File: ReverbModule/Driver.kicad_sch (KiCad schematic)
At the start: 5 parts, among them U1 NE5532

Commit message: In work
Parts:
- added C3, C4, C5, C6: 100nF, Capacitor_SMD:C_0805_2012Metric_Pad1.18x1.45mm_HandSolder, symbol Device:C
- added R3: 20K, symbol Device:R_US
- added RV1: R_Potentiometer_US, symbol Device:R_Potentiometer_US
- added U2: NE5532, symbol Amplifier_Operational:NE5532
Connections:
- net +15V: now also C3.1, C5.1, U2.8 (V+)
- net -15V: now also C4.2, C6.2, U2.4 (V-)
- net GND: now also C3.2, C4.1, C5.2, C6.1, RV1.3
- net at C2.2: now also R3.1, RV1.1
- new net Dry: R3.2
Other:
- title: (none) -> Reverb Driver
- moved on the sheet: C2, U1C

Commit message: In progress
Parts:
- added C7: 100nF, Capacitor_SMD:C_0805_2012Metric_Pad1.18x1.45mm_HandSolder, symbol Device:C
- added R4: 10k, Resistor_SMD:R_0805_2012Metric_Pad1.20x1.40mm_HandSolder, symbol Device:R_US
- added RV2: 20k, symbol Device:R_Potentiometer_Trim_US
- RV1: value R_Potentiometer_US -> 10k
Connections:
- net GND: now also R4.1, RV2.3
- net at U1.5 (+): now also R4.2, RV2.2
- net ToLimiter: now reaches RV1.2
- new net: C7.2, RV2.1
- new net FromLimiter: C7.1
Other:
- note added: "Drive Level"
- moved on the sheet: U1B

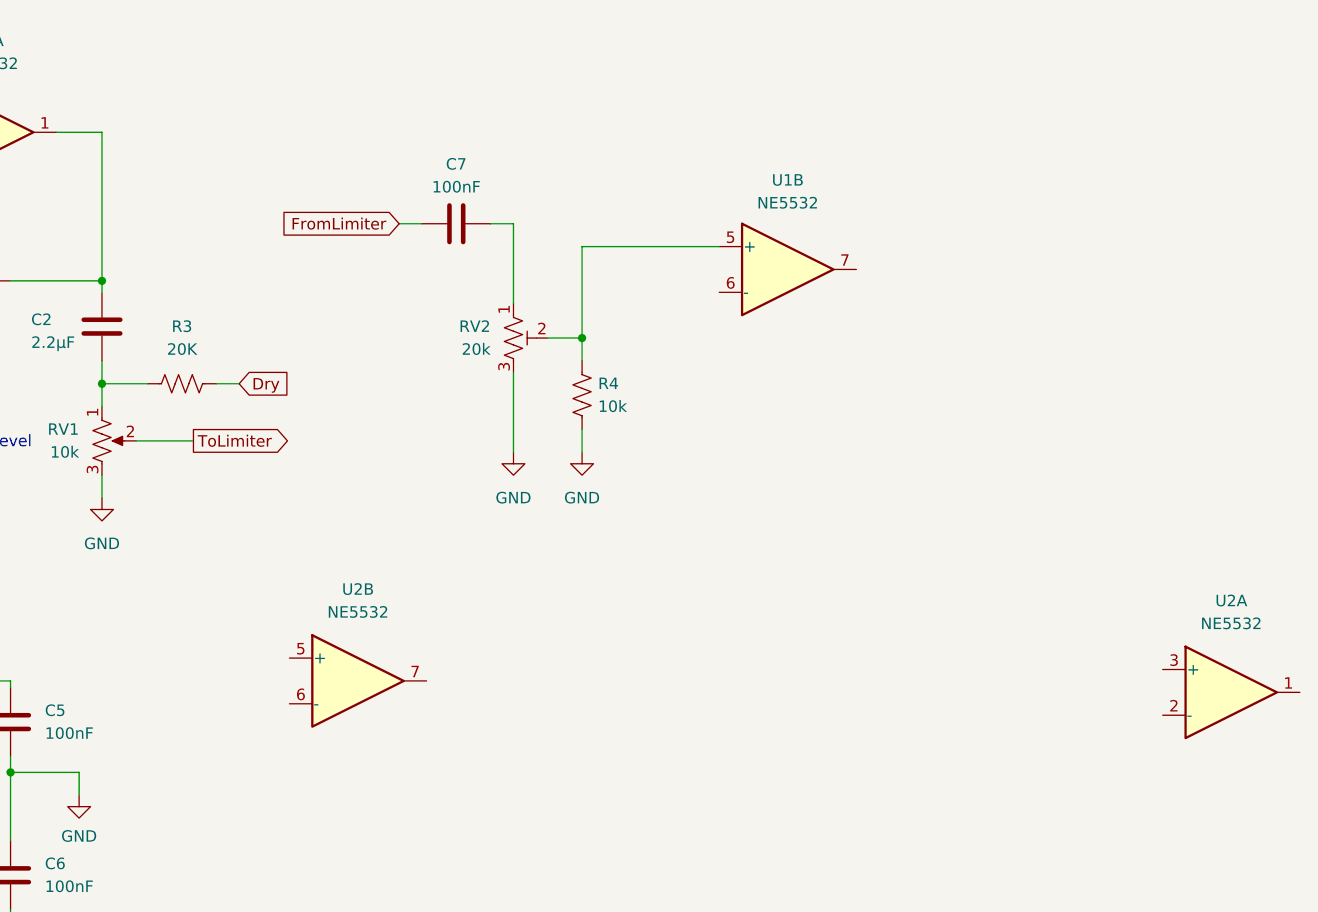
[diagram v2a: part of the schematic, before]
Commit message: added more parts
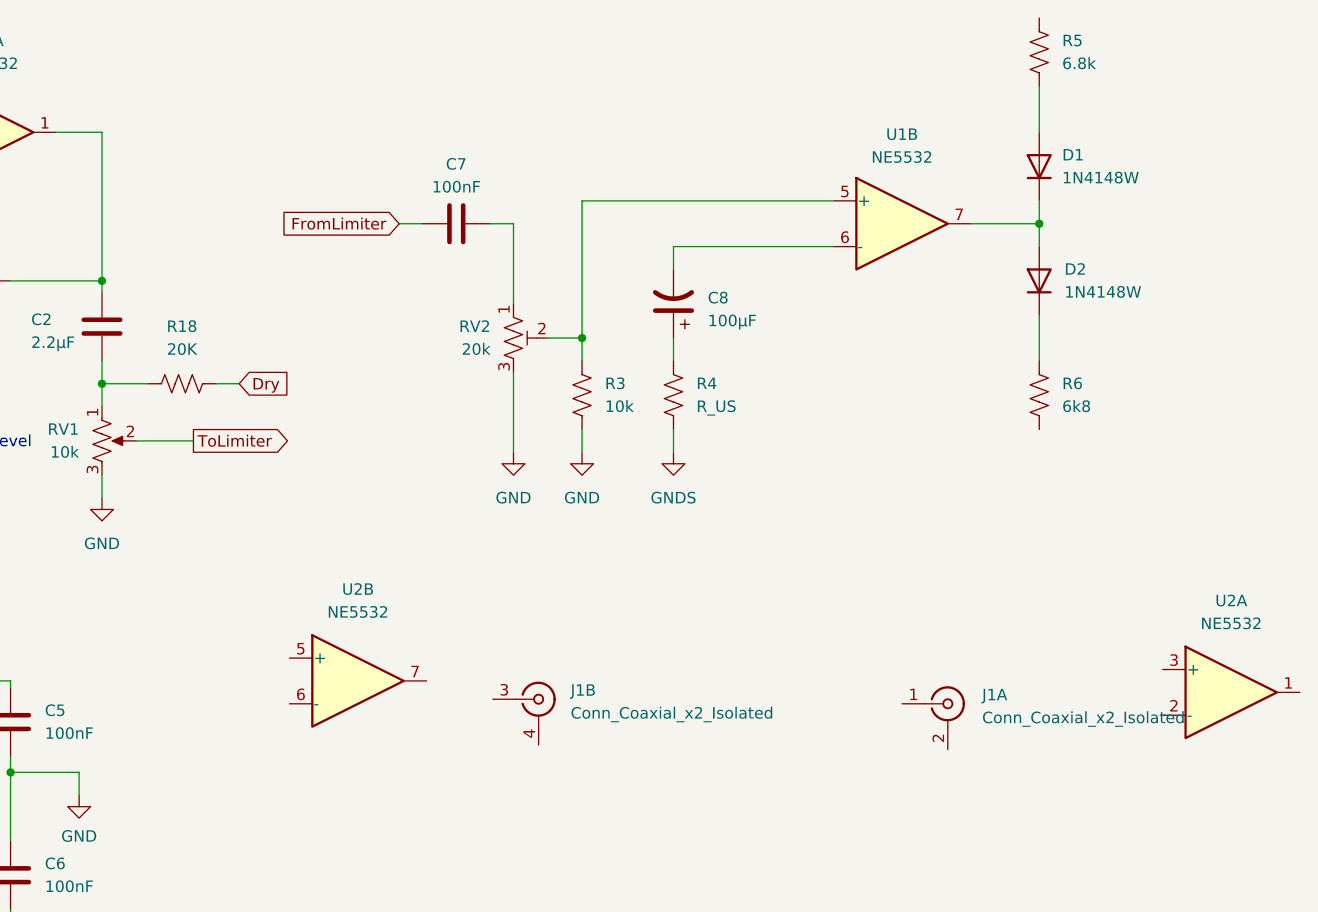
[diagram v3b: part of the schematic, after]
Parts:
- added C8: 100µF, symbol Device:C_Polarized_US
- added D1, D2: 1N4148W, Diode_SMD:D_SOD-123, symbol Diode:1N4148W
- added J1: Conn_Coaxial_x2_Isolated, symbol Connector:Conn_Coaxial_x2_Isolated
- added R4: R_US, symbol Device:R_US
- added R5: 6.8k, Resistor_SMD:R_0805_2012Metric_Pad1.20x1.40mm_HandSolder, symbol Device:R_US
- added R6: 6k8, Resistor_SMD:R_0805_2012Metric_Pad1.20x1.40mm_HandSolder, symbol Device:R_US
- renumbered R3 to R18, R4 to R3
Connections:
- net at U1.6 (-): now also C8.2
- net at U1.7: now also D1.1 (K), D2.2 (A)
- new net: C8.1, R4.1
- new net: D2.1 (K), R6.1
- new net: D1.2 (A), R5.2
- new net GNDS: R4.2
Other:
- moved on the sheet: U1B

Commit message: In worl
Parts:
- removed C1: 2.2µF, Capacitor_SMD:C_1206_3216Metric_Pad1.33x1.80mm_HandSolder, symbol Device:C
- removed unit 2 of J1
- removed unit 2 of U2
- removed unit 1 of U2
- added C1, C10, C9: 10µF, Capacitor_SMD:CP_Elec_5x5.3, symbol Device:C_Polarized_US
- added Q1: BD139, Package_TO_SOT_THT:TO-126-3_Vertical, symbol Transistor_BJT:BD139
- added Q2: BD140, Package_TO_SOT_THT:TO-126-3_Vertical, symbol Transistor_BJT:BD140
- added R7, R8: 10, Resistor_SMD:R_1206_3216Metric_Pad1.30x1.75mm_HandSolder, symbol Device:R_US
- added R9: R_US, symbol Device:R_US
- J1: value Conn_Coaxial_x2_Isolated -> Tank
- R4: value R_US -> 33
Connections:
- net +15V: now also R5.1, Q1.2 (C)
- net -15V: now also R6.2, Q2.1 (E)
- net at C8.2, U1.6 (-): now also R9.2
- net at D1.1 (K), D2.2 (A), U1.7: now also J1.1 (In1), C10.1, C9.2, R7.2, R8.1, R9.1
- net at C8.1, R4.1: now also J1.2 (Ext1)
- net at D2.1 (K), R6.1: now also C10.2, Q2.3 (B)
- net at R1.1: now also C1.2
- net at D1.2 (A), R5.2: now also C9.1, Q1.3 (B)
- new net: Q1.1 (E), R7.1
- new net: Q2.2 (C), R8.2
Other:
- note added: "Tank Input must be floating"
- note added: "pre-order part"
- moved on the sheet: J1A

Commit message: More Schematic Capture
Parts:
- removed C5, C6: 100nF, Capacitor_SMD:C_0805_2012Metric_Pad1.18x1.45mm_HandSolder, symbol Device:C
- removed U2: NE5532, symbol Amplifier_Operational:NE5532
- added C11, C12: 10µF, Capacitor_SMD:CP_Elec_5x5.3, symbol Device:C_Polarized_US
- added J2: Screw_Terminal_01x02, symbol Connector:Screw_Terminal_01x02
- R4: footprint (none) -> Resistor_SMD:R_2512_6332Metric_Pad1.40x3.35mm_HandSolder; LCSC (none) -> C53728; MPN (none) -> 25121WF330JT4E
- R9: value R_US -> 150; footprint (none) -> Resistor_SMD:R_2512_6332Metric_Pad1.40x3.35mm_HandSolder; LCSC (none) -> C25471; MPN (none) -> 25121WJ0151T4E
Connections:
- net +15V: now also C11.1
- net -15V: now also C12.2
- net GND: no longer C3.2, C4.1
- net GNDS: now also C3.2, C4.1, C11.2, C12.1
- net at C1.1: now also J2.2 (Pin_2)
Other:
- moved on the sheet: R9

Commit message: Schematic Capture
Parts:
- J2: footprint (none) -> TerminalBlock_Phoenix:TerminalBlock_Phoenix_MKDS-3-2-5.08_1x02_P5.08mm_Horizontal
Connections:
- net ToLimiter is gone; now on an unnamed net: RV1.2
- net GND: now also J2.1 (Pin_1)
- net FromLimiter: no longer names the net of C7.1
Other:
- moved on the sheet: U1C
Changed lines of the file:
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@@
 	)
 	(junction
-		(at 38.1 119.38)
+		(at 38.1 139.7)
 		(diameter 0)
 		(color 0 0 0 0)
@@
 	)
 	(junction
-		(at 200.66 63.5)
+		(at 38.1 116.84)
 		(diameter 0)
 		(color 0 0 0 0)
 	)
 	(junction
-		(at 203.2 88.9)
+		(at 200.66 63.5)
 		(diameter 0)
 		(color 0 0 0 0)
 	)
 	(junction
-		(at 38.1 142.24)
+		(at 203.2 88.9)
 		(diameter 0)
 		(color 0 0 0 0)
 	)
 	(junction
-		(at 38.1 116.84)
+		(at 38.1 142.24)
 		(diameter 0)
 		(color 0 0 0 0)
@@
 	)
 	(junction
-		(at 38.1 139.7)
-		(diameter 0)
-		(color 0 0 0 0)
-	)
-	(junction
 		(at 60.96 127)
 		(diameter 0)
@@
 	(wire
 		(pts
+			(xy 33.02 72.39) (xy 33.02 76.2)
+		)
+		(stroke
+			(width 0)
+			(type default)
+		)
+	)
+	(wire
+		(pts
+			(xy 114.3 63.5) (xy 114.3 87.63)
+		)
+		(stroke
+			(width 0)
+			(type default)
+		)
+	)
+	(wire
+		(pts
 			(xy 81.28 69.85) (xy 81.28 53.34)
 		)
@@
 	(wire
 		(pts
-			(xy 85.09 87.63) (xy 91.44 87.63)
+			(xy 85.09 87.63) (xy 114.3 87.63)
 		)
 		(stroke
@@
 	(wire
 		(pts
-			(xy 38.1 116.84) (xy 38.1 119.38)
+			(xy 53.34 50.8) (xy 53.34 53.34)
 		)
 		(stroke
@@
 	(wire
 		(pts
-			(xy 53.34 50.8) (xy 53.34 53.34)
+			(xy 144.78 86.36) (xy 144.78 88.9)
 		)
 		(stroke
@@
 	(wire
 		(pts
-			(xy 144.78 86.36) (xy 144.78 88.9)
+			(xy 44.45 69.85) (xy 49.53 69.85)
 		)
 		(stroke
@@
 	(wire
 		(pts
-			(xy 44.45 69.85) (xy 49.53 69.85)
+			(xy 60.96 127) (xy 73.66 127)
 		)
 		(stroke
@@
 	(wire
 		(pts
-			(xy 60.96 127) (xy 73.66 127)
+			(xy 185.42 60.96) (xy 185.42 63.5)
 		)
 		(stroke
@@
 	(wire
 		(pts
-			(xy 185.42 60.96) (xy 185.42 63.5)
+			(xy 152.4 104.14) (xy 152.4 77.47)
 		)
 		(stroke
@@
 	(wire
 		(pts
-			(xy 152.4 104.14) (xy 152.4 77.47)
+			(xy 38.1 137.16) (xy 38.1 139.7)
 		)
 		(stroke
@@
 	(wire
 		(pts
-			(xy 38.1 139.7) (xy 38.1 142.24)
+			(xy 81.28 53.34) (xy 76.2 53.34)
 		)
 		(stroke
@@
 	(wire
 		(pts
-			(xy 81.28 53.34) (xy 76.2 53.34)
+			(xy 38.1 116.84) (xy 38.1 121.92)
 		)
 		(stroke
@@
 	(wire
 		(pts
-			(xy 185.42 76.2) (xy 185.42 78.74)
+			(xy 30.48 72.39) (xy 33.02 72.39)
 		)
 		(stroke
@@
 	(wire
 		(pts
-			(xy 162.56 66.04) (xy 160.02 66.04)
+			(xy 185.42 76.2) (xy 185.42 78.74)
 		)
 		(stroke
@@
 	(wire
 		(pts
-			(xy 220.98 38.1) (xy 220.98 45.72)
+			(xy 162.56 66.04) (xy 160.02 66.04)
 		)
 		(stroke
@@
 	(wire
 		(pts
-			(xy 38.1 134.62) (xy 38.1 139.7)
+			(xy 220.98 38.1) (xy 220.98 45.72)
 		)
 		(stroke
@@
 	(wire
 		(pts
-			(xy 38.1 119.38) (xy 38.1 119.634)
-		)
-		(stroke
-			(width 0)
-			(type default)
-		)
-	)
-	(wire
-		(pts
 			(xy 38.1 111.76) (xy 38.1 114.3)
 		)
@@
 	(wire
 		(pts
+			(xy 38.1 139.7) (xy 38.1 142.24)
+		)
+		(stroke
+			(width 0)
+			(type default)
+		)
+	)
+	(wire
+		(pts
 			(xy 231.14 63.5) (xy 231.14 71.12)
 		)
@@
 		)
 	)
-	(global_label "ToLimiter"
-		(shape output)
-		(at 91.44 87.63 0)
-		(fields_autoplaced yes)
-		(effects
-			(font
-				(size 1.27 1.27)
-			)
-			(justify left)
-		)
-		(property "Intersheetrefs" "${INTERSHEET_REFS}"
-			(at 103.0733 87.63 0)
-			(hide yes)
-			(show_name no)
-			(do_not_autoplace no)
-			(effects
-				(font
-					(size 1.27 1.27)
-				)
-				(justify left)
-			)
-		)
-	)
-	(global_label "FromLimiter"
-		(shape input)
-		(at 114.3 63.5 180)
-		(fields_autoplaced yes)
-		(effects
-			(font
-				(size 1.27 1.27)
-			)
-			(justify right)
-		)
-		(property "Intersheetrefs" "${INTERSHEET_REFS}"
-			(at 100.0662 63.5 0)
-			(hide yes)
-			(show_name no)
-			(do_not_autoplace no)
-			(effects
-				(font
-					(size 1.27 1.27)
-				)
-				(justify right)
-			)
-		)
-	)
 	(global_label "Dry"
 		(shape input)
@@
 			)
 		)
-		(property "Footprint" ""
+		(property "Footprint" "TerminalBlock_Phoenix:TerminalBlock_Phoenix_MKDS-3-2-5.08_1x02_P5.08mm_Horizontal"
 			(at 25.4 72.39 0)
 			(hide yes)
@@
 	(symbol
 		(lib_id "Amplifier_Operational:NE5532")
-		(at 40.64 127 0)
+		(at 40.64 129.54 0)
 		(unit 3)
 		(body_style 1)
@@
 		(fields_autoplaced yes)
 		(property "Reference" "U1"
-			(at 39.116 125.7299 0)
+			(at 39.116 128.2699 0)
 			(show_name no)
 			(do_not_autoplace no)
@@
 		)
 		(property "Value" "NE5532"
-			(at 39.116 128.2699 0)
+			(at 39.116 130.8099 0)
 			(show_name no)
 			(do_not_autoplace no)
@@
 		)
 		(property "Footprint" "Package_SO:SOIC-8_3.9x4.9mm_P1.27mm"
-			(at 40.64 127 0)
+			(at 40.64 129.54 0)
 			(hide yes)
 			(show_name no)
@@
 		)
 		(property "Datasheet" "http://www.ti.com/lit/ds/symlink/ne5532.pdf"
-			(at 40.64 127 0)
+			(at 40.64 129.54 0)
 			(hide yes)
 			(show_name no)
@@
 		)
 		(property "Description" "Dual Low-Noise Operational Amplifiers, DIP-8/SOIC-8"
-			(at 40.64 127 0)
+			(at 40.64 129.54 0)
 			(hide yes)
 			(show_name no)
@@
 		)
 		(property "MPN" "NE5532DR"
-			(at 40.64 127 0)
+			(at 40.64 129.54 0)
 			(hide yes)
 			(show_name no)
@@
 		)
 		(property "LCSC" "C7426"
-			(at 40.64 127 0)
+			(at 40.64 129.54 0)
 			(hide yes)
 			(show_name no)
@@
 					(unit 1)
 				)
+			)
+		)
+	)
+	(symbol
+		(lib_id "power:GND")
+		(at 33.02 76.2 0)
+		(unit 1)
+		(body_style 1)
+		(exclude_from_sim no)
+		(in_bom yes)
+		(on_board yes)
+		(in_pos_files yes)
+		(dnp no)
+		(fields_autoplaced yes)
+		(property "Reference" "#PWR023"
+			(at 33.02 82.55 0)
+			(hide yes)
+			(show_name no)
+			(do_not_autoplace no)
+			(effects
+				(font
+					(size 1.27 1.27)
+				)
+			)
+		)
+		(property "Value" "GND"
+			(at 33.02 81.28 0)
+			(show_name no)
+			(do_not_autoplace no)
+			(effects
+				(font
+					(size 1.27 1.27)
+				)
+			)
+		)
+		(property "Footprint" ""
+			(at 33.02 76.2 0)
+			(hide yes)
+			(show_name no)
+			(do_not_autoplace no)
+			(effects
+				(font
+					(size 1.27 1.27)
+				)
+			)
+		)
+		(property "Datasheet" ""
+			(at 33.02 76.2 0)
+			(hide yes)
+			(show_name no)
+			(do_not_autoplace no)
+			(effects
+				(font
+					(size 1.27 1.27)
+				)
+			)
+		)
+		(property "Description" "Power symbol creates a global label with name \"GND\" , ground"
+			(at 33.02 76.2 0)
+			(hide yes)
+			(show_name no)
+			(do_not_autoplace no)
+			(effects
+				(font
+					(size 1.27 1.27)
+				)
+			)
+		)
+		(pin "1"
+		)
+		(instances
+			(project "ReverbModule"
+				(path "/e19e1d15-f0b3-4286-a818-bc907405212b/c6d45d4c-e85e-4a36-afcc-7c11e84777bd"
+					(reference "#PWR023")
+					(unit 1)
+				)
